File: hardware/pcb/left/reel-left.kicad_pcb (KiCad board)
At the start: 2 copper layers, 145.9 x 95.5 mm, 53 parts, among them J1 Conn_01x02, SW1 SW_Push, SW10 SW_Push, SW11 SW_Push, SW12 SW_Push, SW13 SW_Push, SW14 SW_Push, SW15 SW_Push, SW16 SW_Push, SW17 SW_Push, SW18 SW_Push, SW19 SW_Push, SW2 SW_Push, SW20 SW_Push, SW21 SW_Push, SW22 SW_Push, SW24 SW_SPDT, SW25 RotaryEncoder, SW3 SW_Push, SW4 SW_Push, SW5 SW_Push, SW6 SW_Push, SW7 SW_Push, SW8 SW_Push, SW9 SW_Push

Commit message: Update PCB layouts and mechanical assets
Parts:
- added J2: Conn_01x05, reel:Display_BeeKeeb_MIP_1.08in_LS011B7DH03, F.Cu at (197.5, 95.0)
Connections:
- U1 pad 12: unconnected-(U1-3V3-Pad12) -> 3.3V
- U1 pad 17: unconnected-(U1-NFC3_0.16-Pad17) -> SI
- U1 pad 18: unconnected-(U1-NFC4_1.00-Pad18) -> SCK
- U1 pad 19: unconnected-(U1-NFC5_1.10-Pad19) -> CS

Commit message: Update ReeL hardware and fabrication assets
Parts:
- J1: footprint Connector_JST:JST_PH_S2B-PH-K_1x02_P2.00mm_Horizontal -> reel:JST_S2B-PH-SM4-TB
- SW18: footprint reel:Switch_E-Switch_TS2_Vertical_THT -> reel:Switch_Tactile_6x6x3.5_Vertical_THT_5.08mm
- SW19: footprint reel:Switch_E-Switch_TS2_Vertical_THT_Mirrored -> reel:Switch_Tactile_6x6x3.5_Vertical_THT_5.08mm
- moved J1 5.65 mm to (196.0, 77.4)
- moved SW18 2.24 mm to (217.7, 119.3)
- moved SW19 2.02 mm to (203.2, 144.2)
- moved SW25 0.74 mm to (216.2, 121.7)
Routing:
- net 3.3V: track 0.00 -> 35.8 mm
- net SI: track 0.00 -> 13.9 mm
- net SCK: track 0.00 -> 13.2 mm
- net CS: track 0.00 -> 13.2 mm
- net GND: track 101.0 -> 112.8 mm
- net Net-(D19-A): track 6.41 -> 17.2 mm
- net Col1: track 128.6 -> 121.9 mm
- net Net-(J1-Pin_1): track 13.6 -> 19.0 mm, vias 1 -> 2
- net Net-(D18-A): track 10.0 -> 14.1 mm
- net RotB: track 72.3 -> 69.1 mm
- net RotA: track 62.4 -> 60.5 mm
- net VBAT_SW: track 35.3 -> 36.1 mm
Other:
- board size 145.9 x 95.5 mm -> 145.9 x 95.9 mm

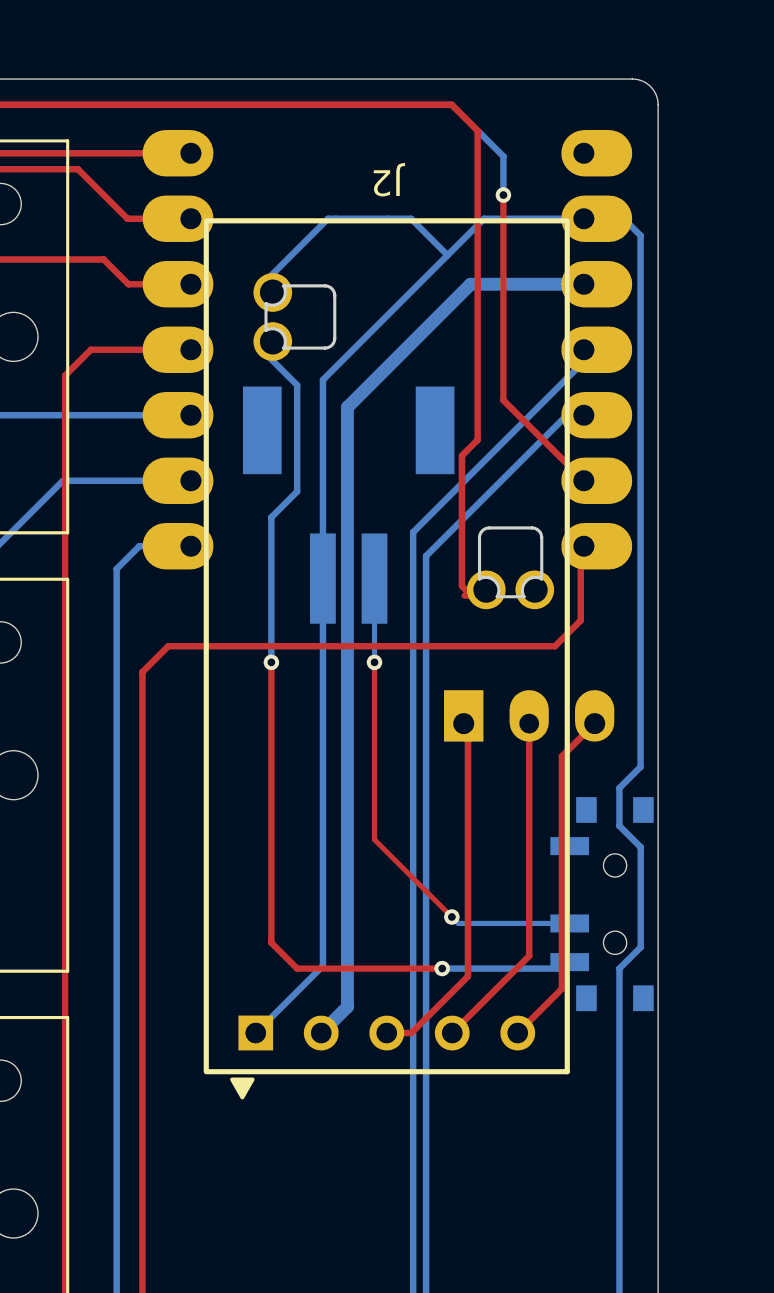
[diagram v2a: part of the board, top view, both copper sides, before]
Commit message: Update hardware assets and trackball profiler
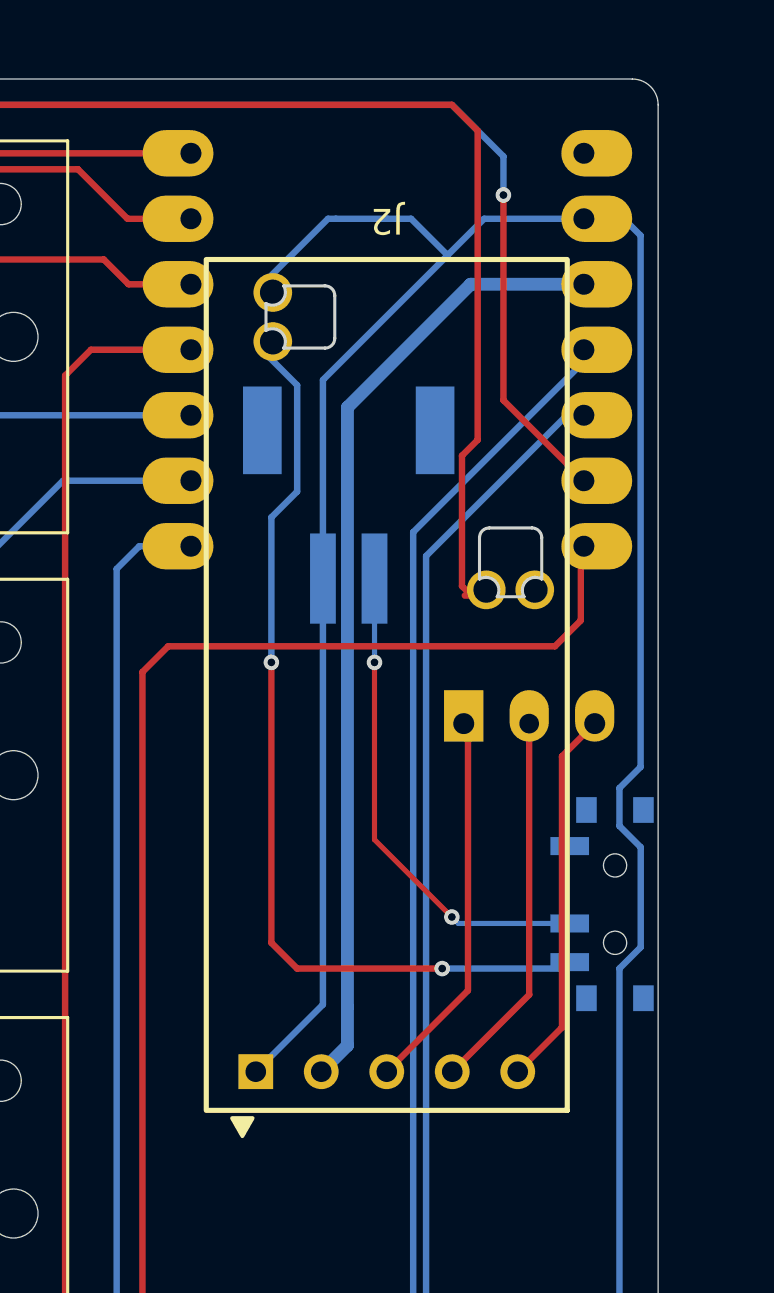
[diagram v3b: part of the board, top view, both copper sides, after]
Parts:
- moved J2 1.50 mm to (197.5, 96.5)
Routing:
- net GND: track 112.8 -> 114.3 mm
- net SCK: track 13.2 -> 14.7 mm
- net CS: track 13.2 -> 14.7 mm
- net 3.3V: track 35.8 -> 37.3 mm
- net SI: track 13.9 -> 14.9 mm
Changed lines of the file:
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@@
 	(footprint "reel:Display_BeeKeeb_MIP_1.08in_LS011B7DH03"
 		(layer "F.Cu")
-		(at 197.475 95 180)
+		(at 197.475 96.5 180)
 		(descr "BeeKeeb 1.08-inch low-power MIP LCD module using Sharp LS011B7DH03; 33 x 14 mm breakout, 5-pin 2.54 mm pitch header; pin 1 GND, 2 VCC, 3 SI, 4 SCK, 5 CS")
 		(tags "BeeKeeb Sharp LS011B7DH03 memory LCD MIP display 1.08 inch 160x68 2.54mm")
@@
 	)
 	(segment
+		(start 195.95 95.485)
+		(end 195.95 93.985)
+		(width 0.5)
+		(layer "B.Cu")
+		(net "3.3V")
+	)
+	(segment
 		(start 200.726828 65.96)
 		(end 195.95 70.736828)
@@
 	)
 	(segment
-		(start 195.95 93.985)
-		(end 194.935 95)
+		(start 194.935 96.5)
+		(end 195.95 95.485)
 		(width 0.5)
 		(layer "B.Cu")
@@
 	)
 	(segment
+		(start 192.395 96.5)
+		(end 195 93.895)
+		(width 0.25)
+		(layer "B.Cu")
+		(net "GND")
+	)
+	(segment
 		(start 216.221156 121.682334)
 		(end 216.221156 119.971156)
@@
 	)
 	(segment
-		(start 195 92.395)
-		(end 192.395 95)
+		(start 195 93.895)
+		(end 195 92.395)
 		(width 0.25)
 		(layer "B.Cu")
@@
 	)
 	(segment
-		(start 197.475 95)
-		(end 198.429594 95)
+		(start 197.475 96.5)
+		(end 200.625 93.35)
 		(width 0.25)
 		(layer "F.Cu")
@@
 	)
 	(segment
-		(start 200.625 92.804594)
-		(end 200.625 83.165)
-		(width 0.25)
-		(layer "F.Cu")
-		(net "SI")
-	)
-	(segment
-		(start 198.429594 95)
-		(end 200.625 92.804594)
+		(start 200.625 83.165)
+		(end 200.625 93.35)
 		(width 0.25)
 		(layer "F.Cu")
@@
 	)
 	(segment
-		(start 200.625 83.165)
-		(end 200.46 83)
+		(start 200.46 83)
+		(end 200.625 83.165)
 		(width 0.25)
 		(layer "F.Cu")
@@
 	)
 	(segment
-		(start 203 92.015)
-		(end 203 83)
+		(start 200.015 96.5)
+		(end 203 93.515)
 		(width 0.25)
 		(layer "F.Cu")
@@
 	)
 	(segment
-		(start 200.015 95)
-		(end 203 92.015)
+		(start 203 93.515)
+		(end 203 83)
 		(width 0.25)
 		(layer "F.Cu")
@@
 	)
 	(segment
-		(start 204.27 93.285)
-		(end 204.27 84.27)
+		(start 204.27 84.27)
+		(end 205.54 83)
 		(width 0.25)
 		(layer "F.Cu")
@@
 	)
 	(segment
-		(start 202.555 95)
-		(end 204.27 93.285)
+		(start 204.27 94.785)
+		(end 204.27 84.27)
 		(width 0.25)
 		(layer "F.Cu")
@@
 	)
 	(segment
-		(start 204.27 84.27)
-		(end 205.54 83)
+		(start 202.555 96.5)
+		(end 204.27 94.785)
 		(width 0.25)
 		(layer "F.Cu")

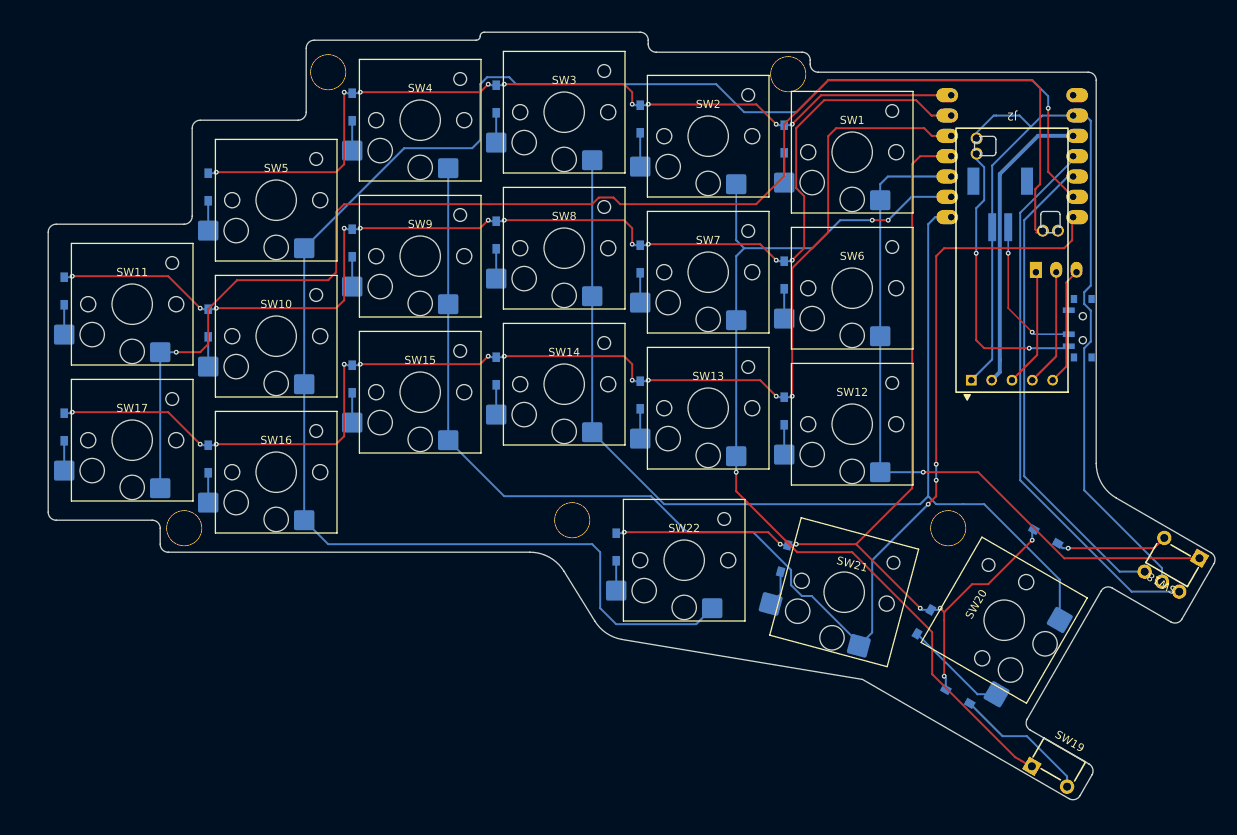
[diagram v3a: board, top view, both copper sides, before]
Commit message: Update PCB routing and mechanical models
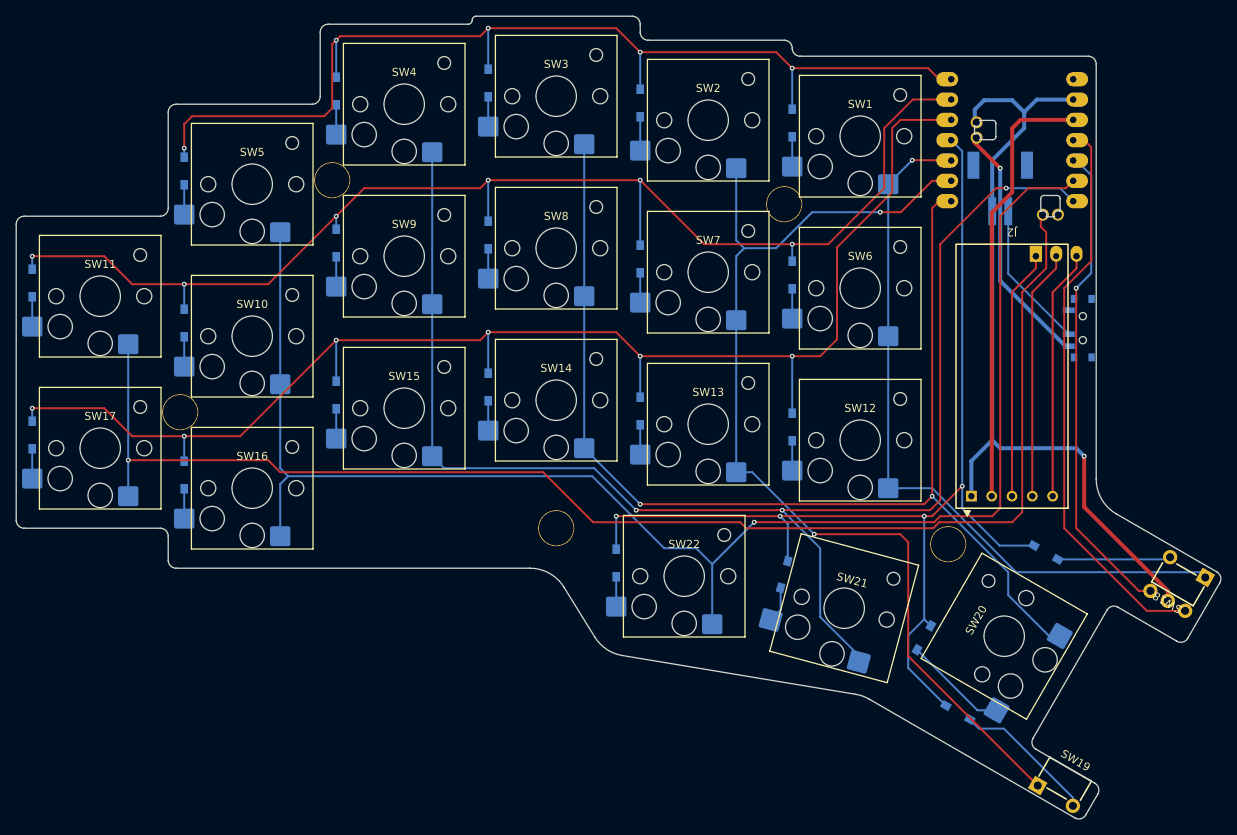
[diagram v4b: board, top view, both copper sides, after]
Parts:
- moved Ref** 16.3 mm to (169.0, 74.5)
- moved Ref** 14.5 mm to (93.5, 100.5)
- moved J2 14.5 mm to (197.5, 111.0)
- moved Ref** 13.5 mm to (112.5, 71.5)
- moved D11 4.12 mm to (75.0, 81.6)
- moved D17 4.12 mm to (75.0, 100.6)
- moved SW11 4.12 mm to (83.5, 86.0)
- moved SW17 4.12 mm to (83.5, 105.0)
- moved D16 3.61 mm to (94.0, 105.6)
- moved D5 3.61 mm to (94.0, 67.6)
- moved SW16 3.61 mm to (102.5, 110.0)
- moved SW5 3.61 mm to (102.5, 72.0)
- moved D10 3.00 mm to (94.0, 86.6)
- moved SW10 3.00 mm to (102.5, 91.0)
- moved D15 2.83 mm to (113.0, 95.6)
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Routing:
- net Col4: track 219.4 -> 190.2 mm
- net Row0: track 107.6 -> 131.8 mm, vias 9 -> 5
- net 3.3V: track 37.3 -> 55.1 mm
- net Row2: track 156.9 -> 173.9 mm, vias 11 -> 6
- net SCK: track 14.7 -> 31.2 mm
- net CS: track 14.7 -> 31.2 mm
- net SI: track 14.9 -> 31.2 mm
- net GND: track 114.3 -> 100.5 mm, vias 0 -> 1
- net Row3: track 127.2 -> 140.0 mm, vias 7 -> 4
- net Row1: track 146.3 -> 158.7 mm, vias 11 -> 6
- net Col3: track 170.7 -> 180.1 mm
- net Col1: track 121.9 -> 130.4 mm, vias 3 -> 2
- net Col2: track 143.2 -> 148.4 mm, vias 0 -> 2
- net VBAT_SW: track 36.1 -> 31.0 mm, vias 2 -> 1
- net RotB: track 69.1 -> 71.0 mm
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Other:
- board size 145.9 x 95.9 mm -> 150.6 x 100.3 mm

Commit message: Update ReeL PCB and mechanical assets
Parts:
- moved J1 1.00 mm to (197.0, 75.4)
- moved J2 1.00 mm to (198.5, 111.0)
- moved SW24 1.00 mm to (207.0, 90.0)
- moved U1 1.00 mm to (198.5, 56.0)
- moved D2 0.43 mm to (151.0, 59.5)
- moved D1 0.07 mm to (170.0, 61.5)
- moved D3 0.07 mm to (132.0, 56.5)
- moved D4 0.07 mm to (113.0, 57.5)
- moved D10 0.07 mm to (94.0, 86.5)
- moved D11 0.07 mm to (75.0, 81.5)
- moved D12 0.07 mm to (170.0, 99.5)
- moved D13 0.07 mm to (151.0, 97.5)
- moved D14 0.07 mm to (132.0, 94.5)
- moved D15 0.07 mm to (113.0, 95.5)
- moved D16 0.07 mm to (94.0, 105.5)
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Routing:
- net RotB: track 71.0 -> 72.8 mm
- net RotA: track 60.4 -> 61.8 mm
- net Row0: track 131.8 -> 132.9 mm
- net Col0: track 91.4 -> 92.5 mm
- net Col2: track 148.4 -> 149.4 mm
- net Col1: track 130.4 -> 131.4 mm
- net GND: track 100.5 -> 99.5 mm
- net Row3: track 140.0 -> 140.9 mm
- net Col3: track 180.1 -> 180.9 mm
- net Col5: track 173.6 -> 174.1 mm
- net Col4: track 190.2 -> 190.8 mm
- net Row2: track 173.9 -> 174.4 mm
- net Row1: track 158.7 -> 159.2 mm
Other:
- outline, holes or cut-outs redrawn

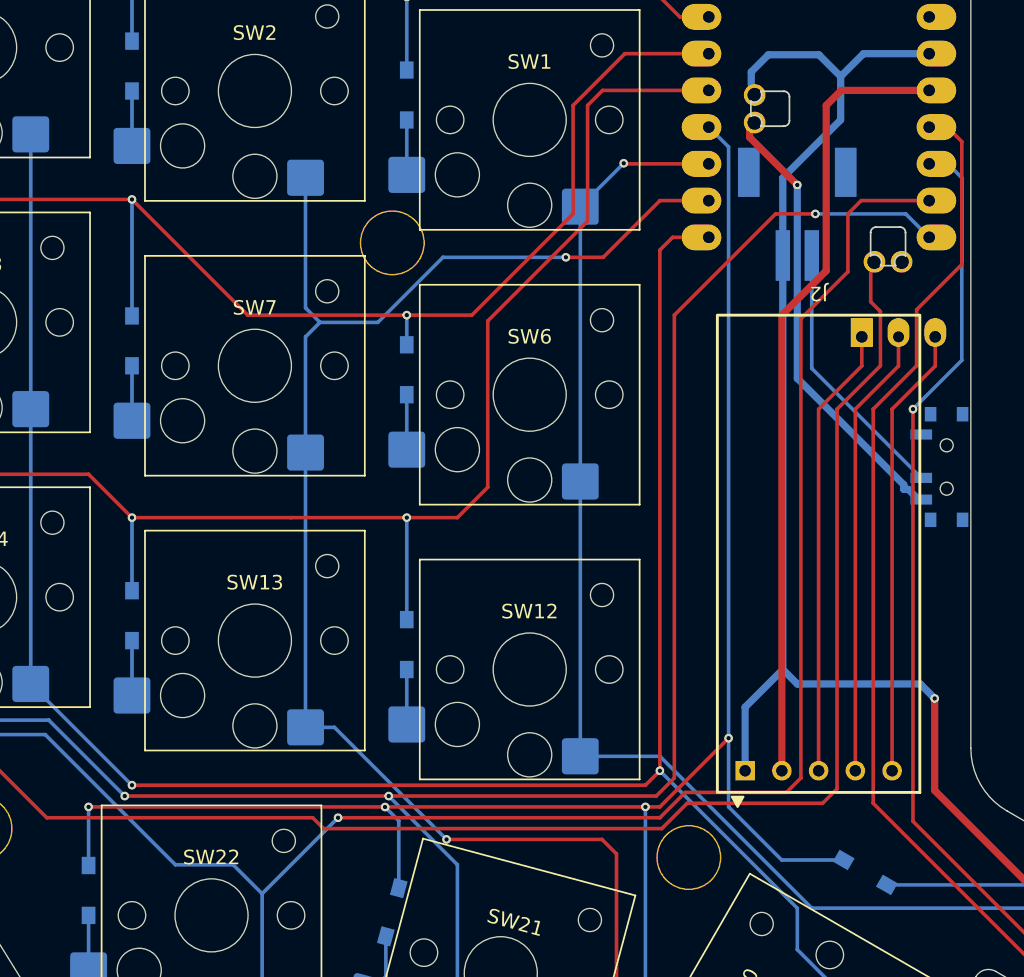
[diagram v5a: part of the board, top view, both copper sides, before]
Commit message: Correct ReeL PCB connector pinouts and routing
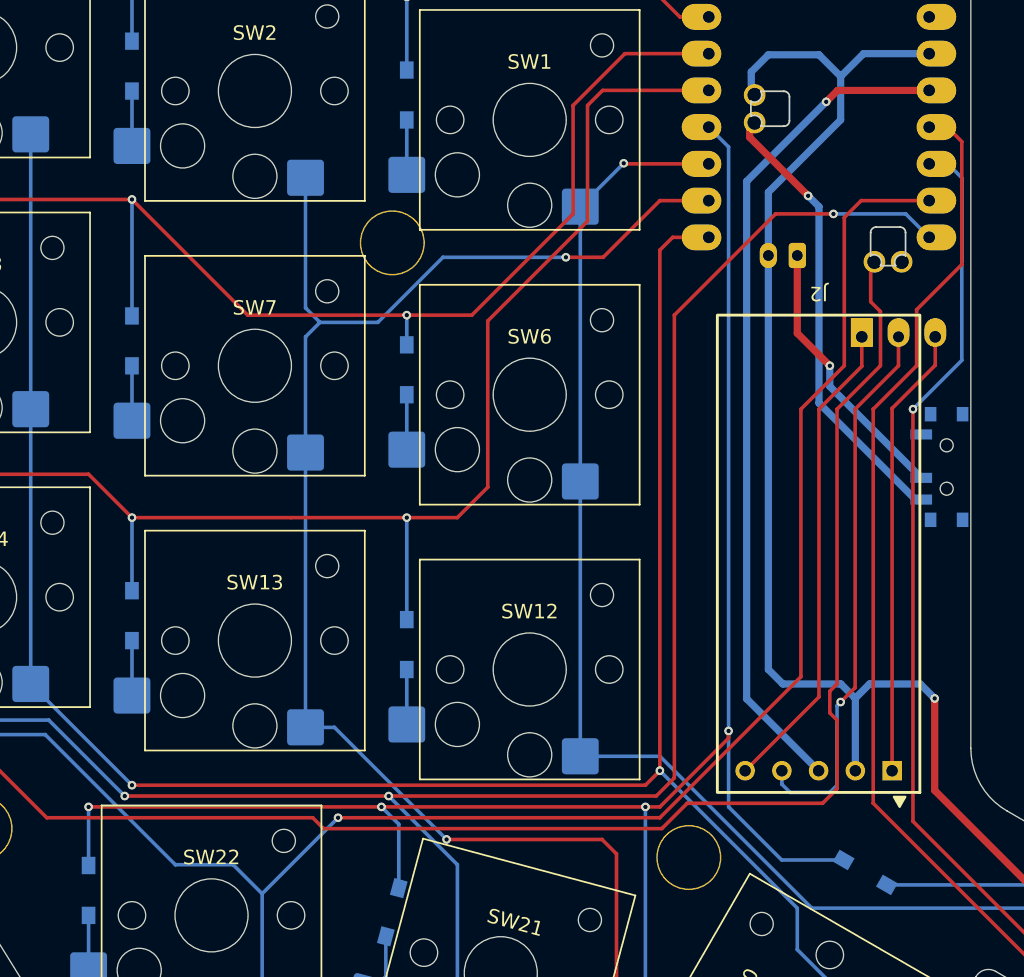
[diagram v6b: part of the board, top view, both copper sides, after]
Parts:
- J1: footprint reel:JST_S2B-PH-SM4-TB -> Connector_JST:JST_PH_S2B-PH-K_1x02_P2.00mm_Horizontal
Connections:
- J2 pad 1: GND -> SI
- J2 pad 2: 3.3V -> SCK
- J2 pad 3: SI -> 3.3V
- J2 pad 4: SCK -> GND
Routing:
- net SCK: track 31.2 -> 38.0 mm, vias 0 -> 1
- net Col4: track 190.8 -> 186.7 mm
- net 3.3V: track 54.8 -> 58.0 mm, vias 0 -> 1
- net SI: track 31.2 -> 33.3 mm
- net GND: track 99.5 -> 98.8 mm
- net Row3: track 140.9 -> 141.6 mm
- net Net-(J1-Pin_1): track 18.5 -> 18.9 mm, vias 0 -> 1

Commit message: Update left and right PCB routing
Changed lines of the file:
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@@
 			(layer "F.Fab")
 		)
-		(fp_text user "GND"
-			(at 5.08 1.5 90)
+		(fp_text user "SI"
+			(at 5 1.25 90)
 			(layer "F.Fab")
 			(effects
@@
 			)
 		)
-		(fp_text user "VCC"
-			(at 2.54 1.5 90)
+		(fp_text user "SCK"
+			(at 2.5 1.5 90)
 			(layer "F.Fab")
 			(effects
@@
 			)
 		)
-		(fp_text user "SI"
-			(at 0 1.25 90)
+		(fp_text user "VCC"
+			(at 0 1.5 90)
 			(layer "F.Fab")
 			(effects
@@
 			)
 		)
-		(fp_text user "SCK"
-			(at -2.54 1.5 90)
+		(fp_text user "GND"
+			(at -2.5 1.5 90)
 			(layer "F.Fab")
 			(effects
@@
 		(width 0.5)
 		(layer "B.Cu")
-		(net "GND")
-	)
-	(segment
-		(start 201.015 106)
-		(end 201.015 105.985)
-		(width 0.5)
-		(layer "B.Cu")
